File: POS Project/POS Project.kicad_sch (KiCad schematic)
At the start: 31 parts, among them J1 JST_2mm_LiPo, P1 USB_C_Plug_USB2.0, U1 MCP73831-2-OT, U2 SMN-303, U4 SMF05C

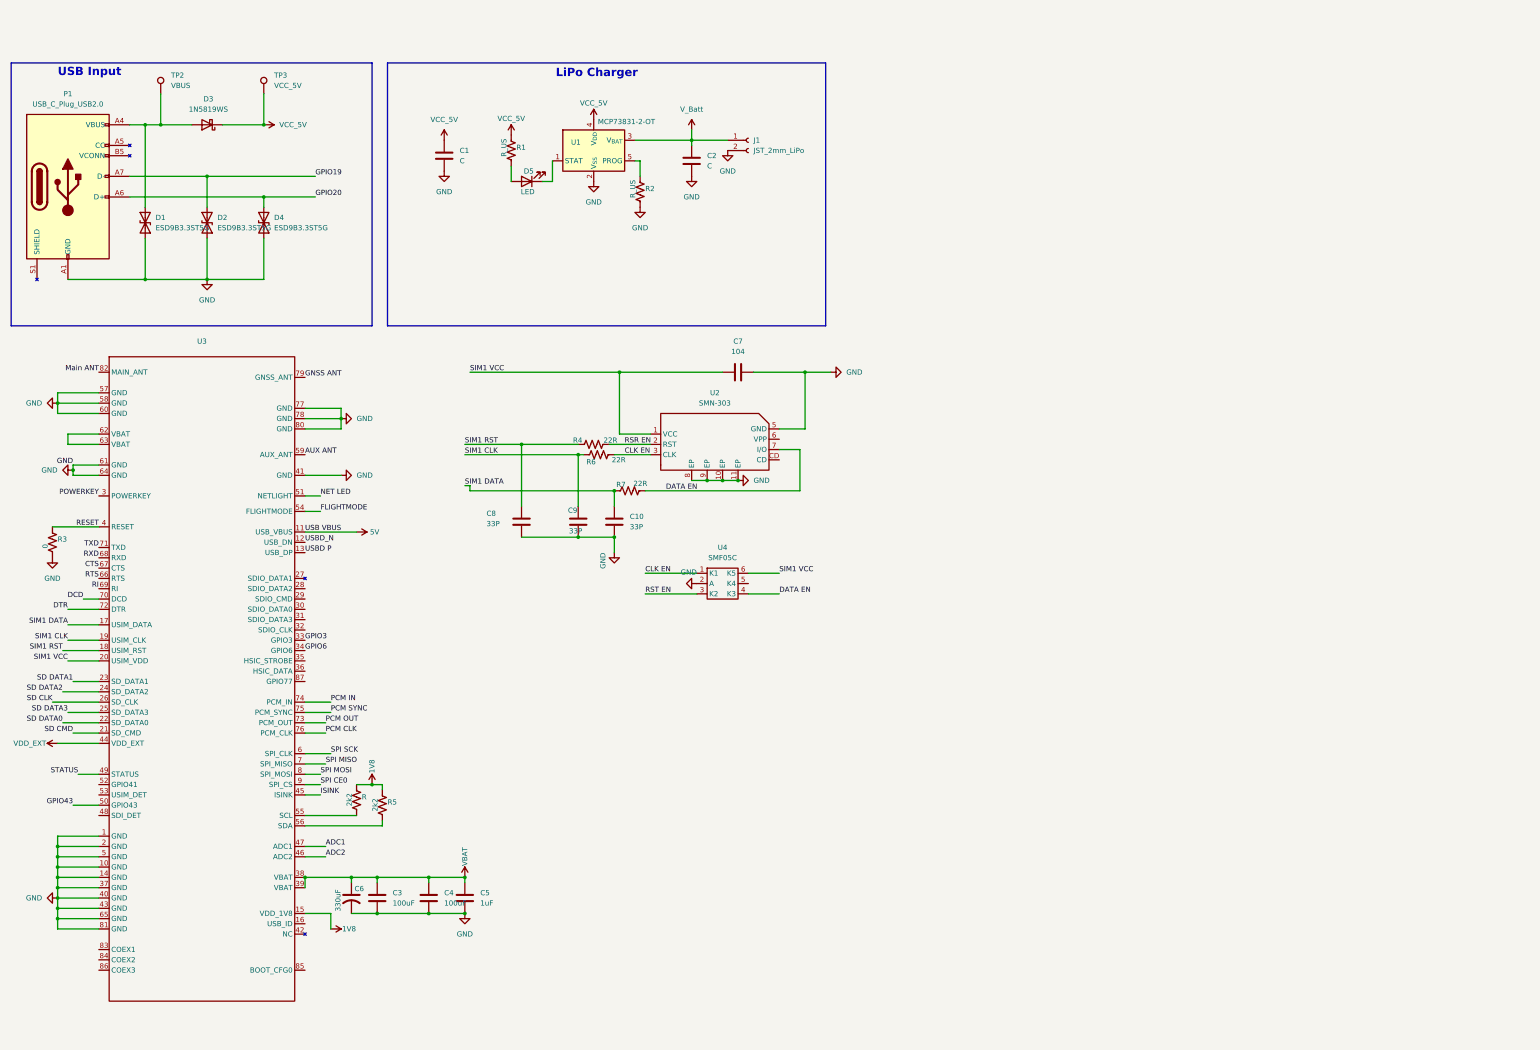
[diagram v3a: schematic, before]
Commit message: added esp32s3
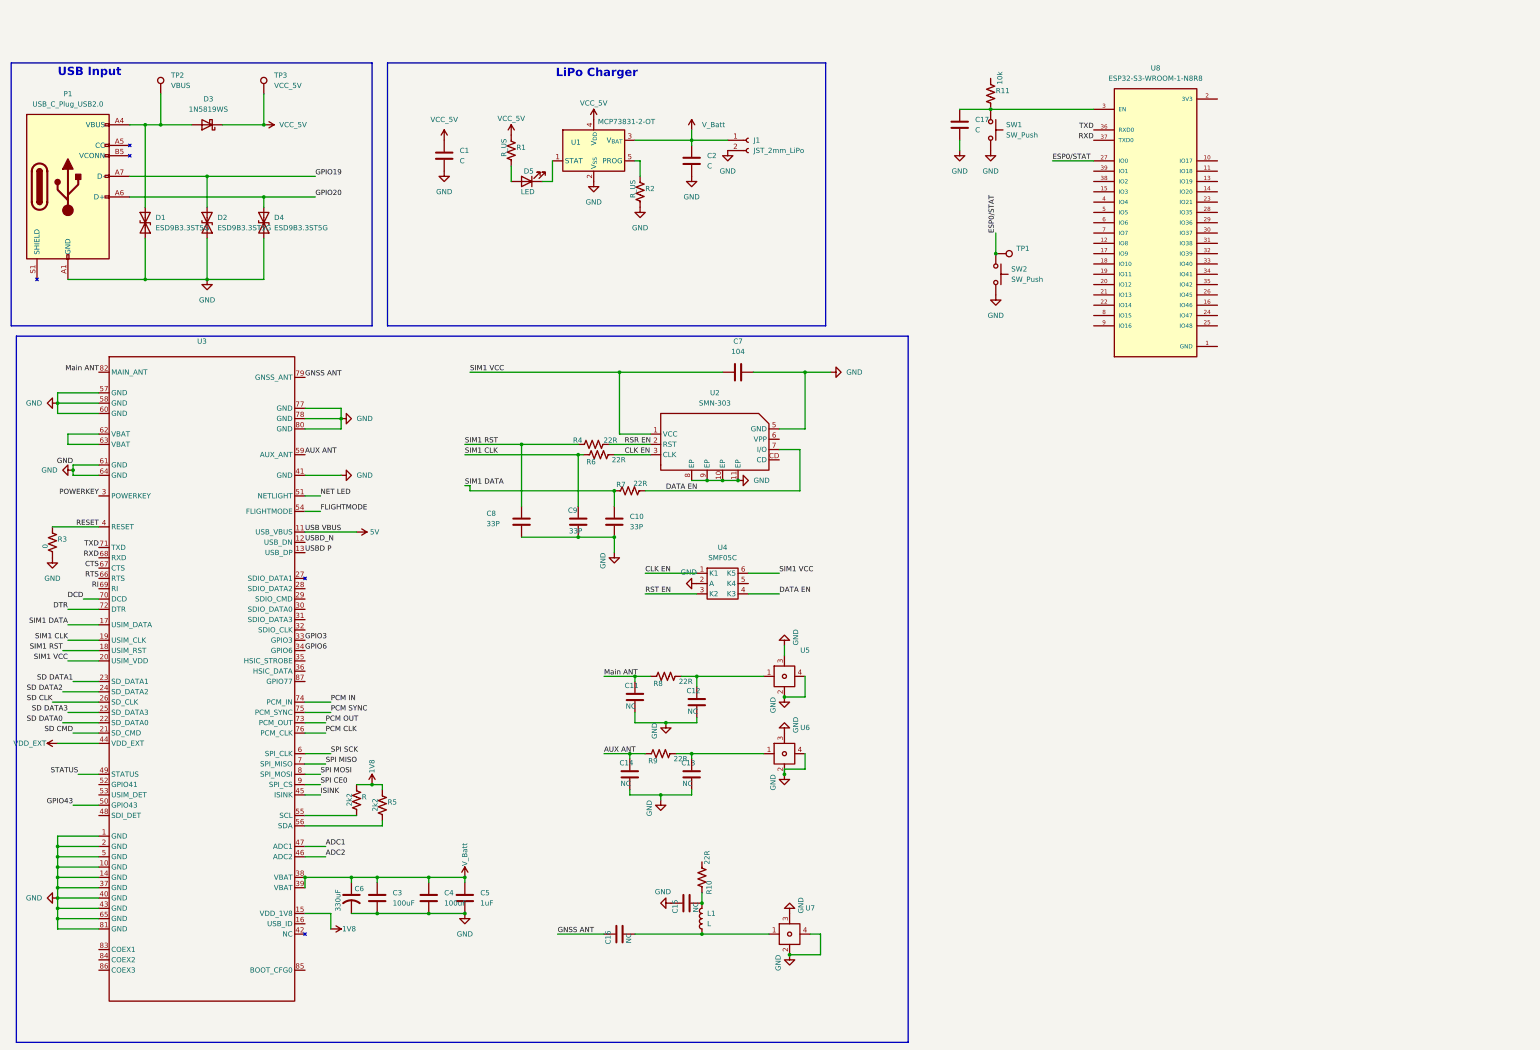
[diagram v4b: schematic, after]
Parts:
- added C11, C12, C13, C14, C15, C16: NC, symbol Device:C
- added C17: C, symbol Device:C
- added L1: L, symbol Device:L
- added R10, R8, R9: 22R, symbol Device:R_US
- added R11: 10k, symbol Device:R_US
- added SW1, SW2: SW_Push, symbol Switch:SW_Push
- added TP1: ~, symbol Connector:TestPoint
- added U5, U6, U7: ~, symbol POSproject:BWIPX-4-0001E
- added U8: ESP32-S3-WROOM-1-N8R8, ESP32-S3-WROOM-1-N8R8:XCVR_ESP32S3WROOM1N8R8, symbol ESP32-S3-WROOM-1-N8R8:ESP32-S3-WROOM-1-N8R8
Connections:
- net VBAT is gone; now on net V_Batt: C3.1, C4.1, C5.1, C6.1, U3.38 (VBAT), U3.39 (VBAT)
- net AUX ANT: now also C14.2, R9.1
- net GND: now also C11.1, C12.1, C13.1, C14.1, C15.2, C17.2, SW1.2, SW2.2, U5.2, U5.3, U5.4, U6.2, U6.3, U6.4, U7.2, U7.3, U7.4, U8.1 (GND), U8.40 (GND), U8.41_1 (GND), U8.41_2 (GND), U8.41_3 (GND), U8.41_4 (GND), U8.41_5 (GND), U8.41_6 (GND), U8.41_7 (GND), U8.41_8 (GND), U8.41_9 (GND)
- net GNSS ANT: now also C16.2
- net Main ANT: now also C11.2, R8.1
- net RXD: now also U8.37 (TXD0)
- net TXD: now also U8.36 (RXD0)
- new net: C12.2, R8.2, U5.1
- new net: C17.1, R11.2, SW1.1, U8.3 (EN)
- new net: C13.2, R9.2, U6.1
- new net: C15.1, L1.2, R10.1
- new net: C16.1, L1.1, U7.1
- new net ESP0/STAT: SW2.1, TP1.1, U8.27 (IO0)

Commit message: added esp32s3, voltage reg, magtek schematic
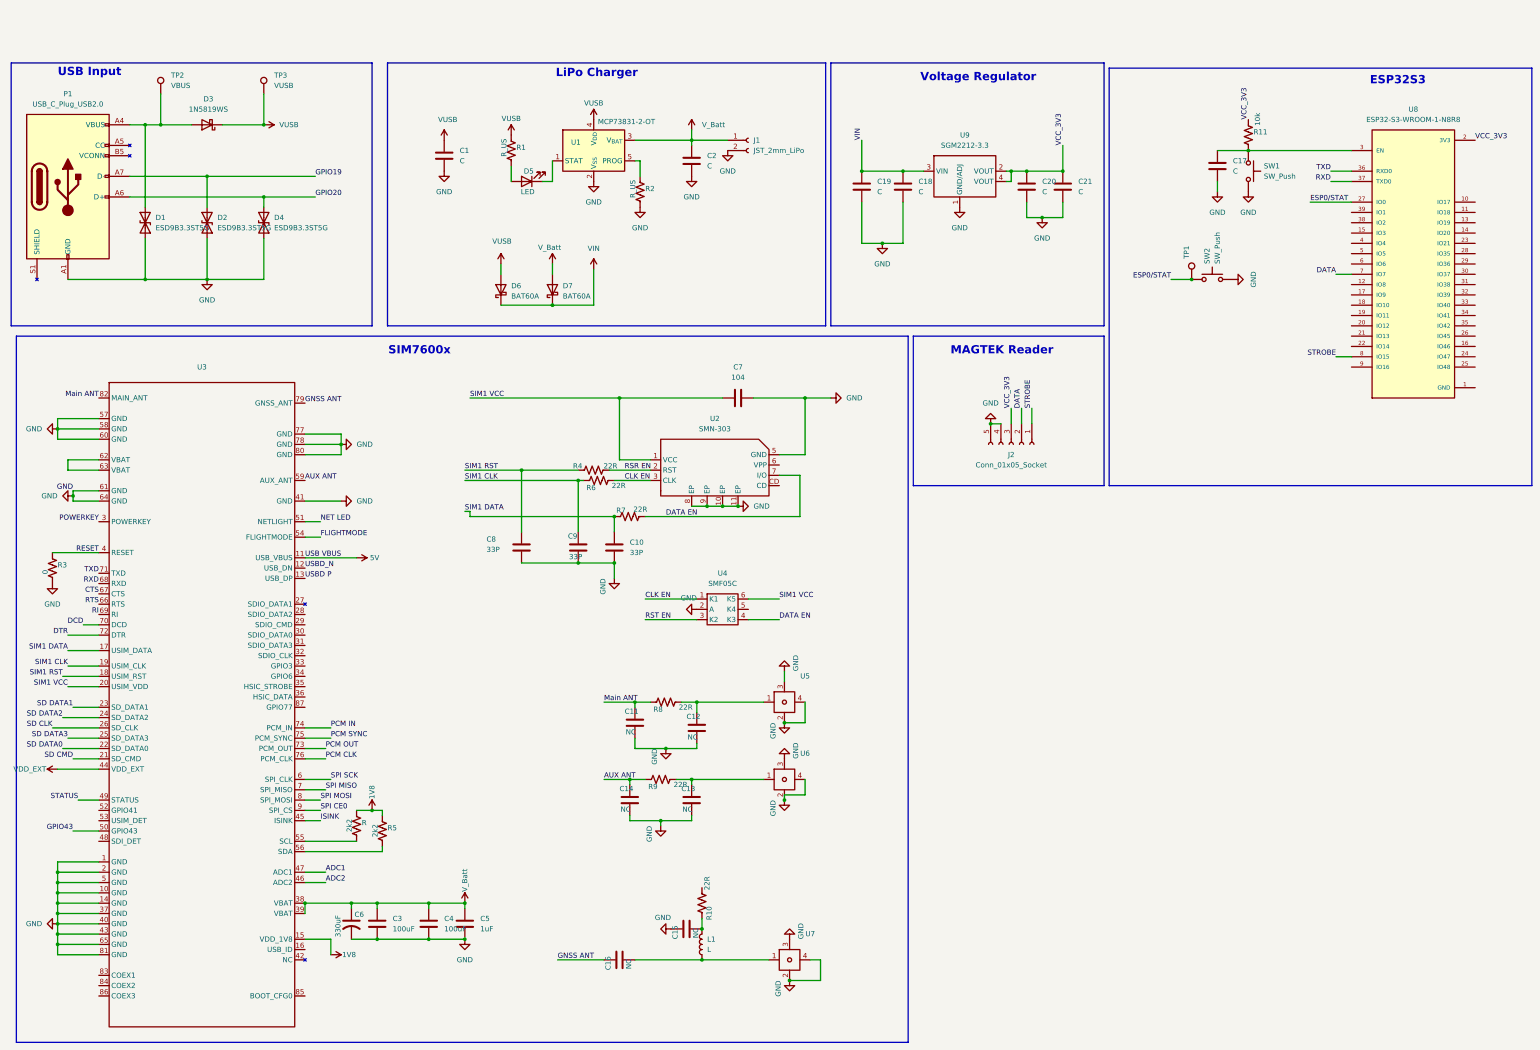
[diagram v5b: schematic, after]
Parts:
- added C18, C19, C20, C21: C, symbol Device:C
- added D6, D7: BAT60A, Diode_SMD:D_SOD-323, symbol Diode:BAT60A
- added J2: Conn_01x05_Socket, symbol POSproject:MAGTEK_connector
- added U9: SGM2212-3.3, Package_TO_SOT_SMD:SOT-223, symbol POSproject:SGM2212-3.3
- TP3: value VCC_5V -> VUSB
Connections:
- net GND: now also C18.2, C19.2, C20.2, C21.2, J2.4 (GND), J2.5 (CASE), U9.1 (GND/ADJ)
- net V_Batt: now also D7.2 (A)
- net VCC_3V3: now reaches R11.1
- net VCC_3V3: now also U8.2 (3V3), C20.1, C21.1, J2.3 (VDD), U9.2 (VOUT), U9.4 (VOUT)
- net DATA: now reaches U8.7 (IO7)
- net DATA: now also J2.2 (DATA)
- net STROBE: now reaches U8.8 (IO15)
- net STROBE: now also J2.1 (STROBE)
- net GPIO3: no longer names the net of U3.33 (GPIO3)
- net GPIO6: no longer names the net of U3.34 (GPIO6)
- net VCC_5V renamed VUSB
- net VUSB: now also D6.2 (A)
- new net VIN: C18.1, C19.1, D6.1 (K), D7.1 (K), U9.3 (VIN)
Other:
- note added: "ESP32S3"
- note added: "MAGTEK Reader"
- note added: "SIM7600x"
- note added: "Voltage Regulator"
- moved on the sheet: C10, C11, C12, C13, C14, C15, C16, C17, C3, C4, C5, C6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

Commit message: Added footprints for some of the components
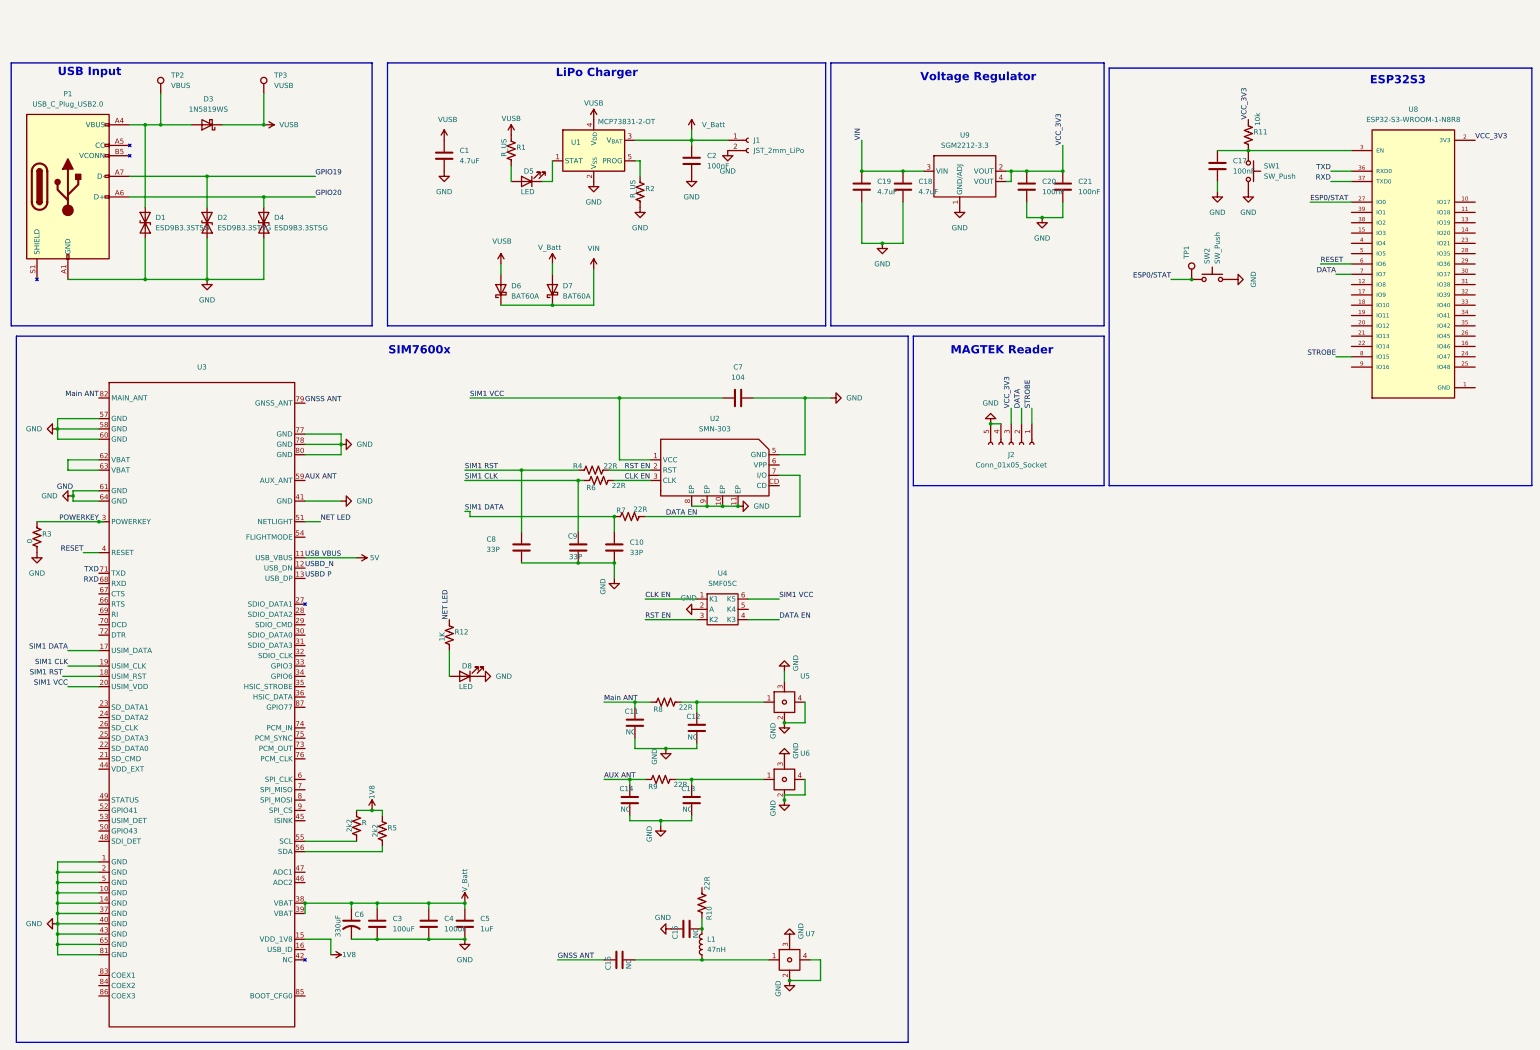
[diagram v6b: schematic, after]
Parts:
- added D8: LED, LED_SMD:LED_0805_2012Metric, symbol Device:LED
- added R12: 1K, symbol Device:R_US
- C1, C18, C19: value C -> 4.7uF
- C10, C11, C12, C13, C14, C15, C16, C3, C4, C5, C7, C8, C9: footprint (none) -> Capacitor_SMD:C_0805_2012Metric
- C17, C2, C20, C21: value C -> 100nF; footprint (none) -> Capacitor_SMD:C_0805_2012Metric
- C6: footprint (none) -> Capacitor_SMD:CP_Elec_10x12.5
- D5: footprint (none) -> LED_SMD:LED_0805_2012Metric
- J1: footprint (none) -> Connector_TE-Connectivity:TE_440054-2_1x02_P2.00mm_Vertical
- J2: footprint (none) -> Connector_Molex:Molex_PicoBlade_53047-0510_1x05_P1.25mm_Vertical
- L1: value L -> 47nH; footprint (none) -> Inductor_SMD:L_0805_2012Metric
- P1, R1, R2: footprint (none) -> Connector_USB:USB_C_Receptacle_GCT_USB4105-xx-A_16P_TopMnt_Horizontal
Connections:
- net RSR EN is gone; now on net RST EN: R4.2, U2.2 (RST)
- net GND: now also D8.1 (K)
- net NET LED: now also R12.1
- net POWERKEY: now also R3.1
- net RESET: now also U8.6 (IO6); no longer R3.1
- net ADC1: no longer names the net of U3.47 (ADC1)
- net ADC2: no longer names the net of U3.46 (ADC2)
- net CTS: no longer names the net of U3.67 (CTS)
- net DCD: no longer names the net of U3.70 (DCD)
- net DTR: no longer names the net of U3.72 (DTR)
- net FLIGHTMODE: no longer names the net of U3.54 (FLIGHTMODE)
- net GPIO43: no longer names the net of U3.50 (GPIO43)
- net ISINK: no longer names the net of U3.45 (ISINK)
- net PCM CLK: no longer names the net of U3.76 (PCM_CLK)
- net PCM IN: no longer names the net of U3.74 (PCM_IN)
- net PCM OUT: no longer names the net of U3.73 (PCM_OUT)
- net PCM SYNC: no longer names the net of U3.75 (PCM_SYNC)
- net RI: no longer names the net of U3.69 (RI)
- net RTS: no longer names the net of U3.66 (RTS)
- net SD CLK: no longer names the net of U3.26 (SD_CLK)
- net SD CMD: no longer names the net of U3.21 (SD_CMD)
- net SD DATA0: no longer names the net of U3.22 (SD_DATA0)
- net SD DATA1: no longer names the net of U3.23 (SD_DATA1)
- net SD DATA2: no longer names the net of U3.24 (SD_DATA2)
- net SD DATA3: no longer names the net of U3.25 (SD_DATA3)
- net SPI CE0: no longer names the net of U3.9 (SPI_CS)
- net SPI MISO: no longer names the net of U3.7 (SPI_MISO)
- net SPI MOSI: no longer names the net of U3.8 (SPI_MOSI)
- net SPI SCK: no longer names the net of U3.6 (SPI_CLK)
- net STATUS: no longer names the net of U3.49 (STATUS)
- net VDD_EXT: no longer names the net of U3.44 (VDD_EXT)
- new net: D8.2 (A), R12.2
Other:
- moved on the sheet: R3
